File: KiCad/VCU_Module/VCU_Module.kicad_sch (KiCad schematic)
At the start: 5 parts, among them J1 5810132011, J5 pin header, J7 5V, J8 3V3, J9 GND

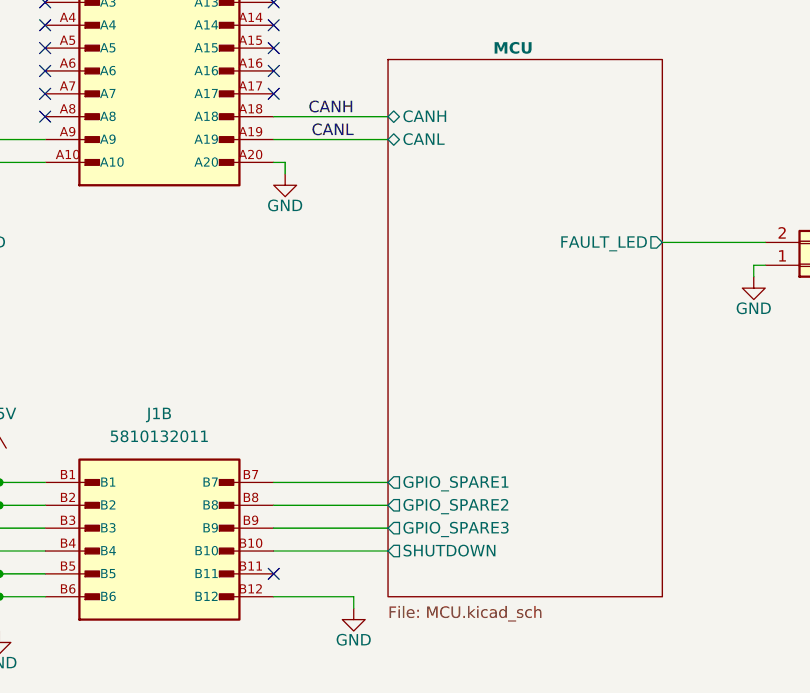
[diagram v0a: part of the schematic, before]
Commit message: added peripherals to mcu
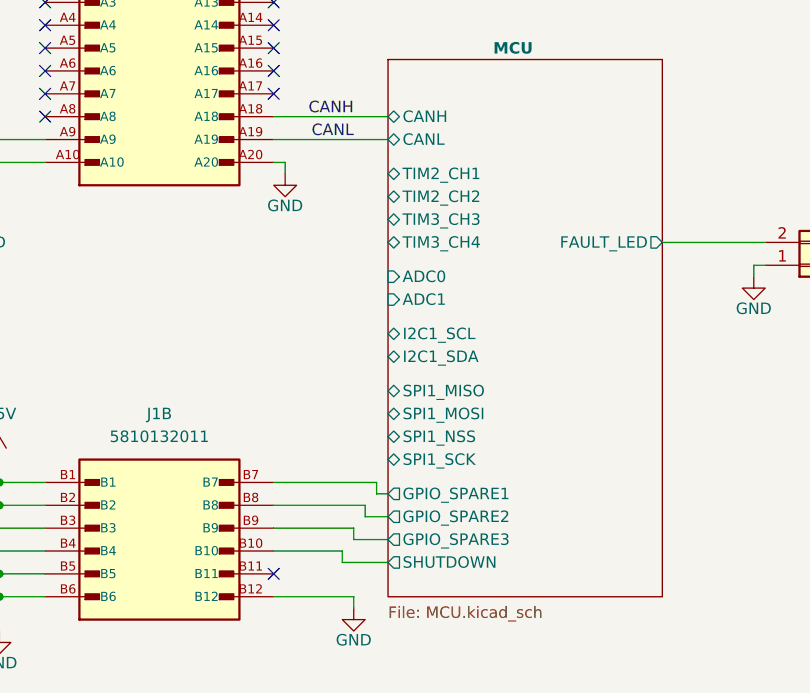
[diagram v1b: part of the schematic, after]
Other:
- sheet MCU ports: added ADC0, ADC1, I2C1_SCL, I2C1_SDA, SPI1_MISO, SPI1_MOSI, SPI1_NSS, SPI1_SCK, TIM2_CH1, TIM2_CH2, TIM3_CH3, TIM3_CH4; removed none
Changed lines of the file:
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@@
+	(wire
+		(pts
+			(xy 300.99 177.8) (xy 300.99 176.53)
+		)
+		(stroke
+			(width 0)
+			(type default)
+		)
+	)
+	(wire
+		(pts
+			(xy 297.18 185.42) (xy 297.18 184.15)
+		)
+		(stroke
+			(width 0)
+			(type default)
+		)
+	)
 	(wire
 		(pts
@@
 	(wire
 		(pts
+			(xy 299.72 180.34) (xy 299.72 179.07)
+		)
+		(stroke
+			(width 0)
+			(type default)
+		)
+	)
+	(wire
+		(pts
 			(xy 259.08 186.69) (xy 259.08 189.23)
 		)
@@
 	(wire
 		(pts
-			(xy 289.56 184.15) (xy 302.26 184.15)
+			(xy 297.18 185.42) (xy 302.26 185.42)
 		)
 		(stroke
@@
 	(wire
 		(pts
+			(xy 300.99 176.53) (xy 289.56 176.53)
+		)
+		(stroke
+			(width 0)
+			(type default)
+		)
+	)
+	(wire
+		(pts
 			(xy 346.71 106.68) (xy 345.44 106.68)
 		)
@@
 	(wire
 		(pts
-			(xy 289.56 176.53) (xy 302.26 176.53)
+			(xy 300.99 177.8) (xy 302.26 177.8)
 		)
 		(stroke
@@
 	(wire
 		(pts
-			(xy 289.56 179.07) (xy 302.26 179.07)
+			(xy 299.72 180.34) (xy 302.26 180.34)
 		)
 		(stroke
@@
 	(wire
 		(pts
+			(xy 298.45 182.88) (xy 298.45 181.61)
+		)
+		(stroke
+			(width 0)
+			(type default)
+		)
+	)
+	(wire
+		(pts
 			(xy 257.81 138.43) (xy 264.16 138.43)
 		)
@@
 	(wire
 		(pts
+			(xy 299.72 179.07) (xy 289.56 179.07)
+		)
+		(stroke
+			(width 0)
+			(type default)
+		)
+	)
+	(wire
+		(pts
 			(xy 259.08 173.99) (xy 259.08 176.53)
 		)
@@
 	(wire
 		(pts
-			(xy 289.56 181.61) (xy 302.26 181.61)
+			(xy 298.45 182.88) (xy 302.26 182.88)
 		)
 		(stroke
@@
 	(wire
 		(pts
+			(xy 298.45 181.61) (xy 289.56 181.61)
+		)
+		(stroke
+			(width 0)
+			(type default)
+		)
+	)
+	(wire
+		(pts
 			(xy 257.81 140.97) (xy 257.81 138.43)
 		)
@@
 		(pts
 			(xy 345.44 114.3) (xy 346.71 114.3)
+		)
+		(stroke
+			(width 0)
+			(type default)
+		)
+	)
+	(wire
+		(pts
+			(xy 297.18 184.15) (xy 289.56 184.15)
 		)
 		(stroke
@@
 		)
 		(pin "SHUTDOWN" output
-			(at 302.26 184.15 180)
+			(at 302.26 185.42 180)
 			(effects
 				(font
@@
 		)
 		(pin "GPIO_SPARE1" output
-			(at 302.26 176.53 180)
+			(at 302.26 177.8 180)
 			(effects
 				(font
@@
 		)
 		(pin "GPIO_SPARE3" output
-			(at 302.26 181.61 180)
+			(at 302.26 182.88 180)
 			(effects
 				(font
@@
 		)
 		(pin "GPIO_SPARE2" output
-			(at 302.26 179.07 180)
+			(at 302.26 180.34 180)
 			(effects
 				(font
@@
 			(effects
 				(font
+					(size 1.27 1.27)
+				)
+				(justify left)
+			)
+		)
+		(pin "ADC0" input
+			(at 302.26 153.67 180)
+			(effects
+				(font
+					(size 1.27 1.27)
+				)
+				(justify left)
+			)
+		)
+		(pin "ADC1" input
+			(at 302.26 156.21 180)
+			(effects
+				(font
+					(size 1.27 1.27)
+				)
+				(justify left)
+			)
+		)
+		(pin "I2C1_SCL" bidirectional
+			(at 302.26 160.02 180)
+			(effects
+				(font
+					(size 1.27 1.27)
+				)
+				(justify left)
+			)
+		)
+		(pin "I2C1_SDA" bidirectional
+			(at 302.26 162.56 180)
+			(effects
+				(font
+					(size 1.27 1.27)
+				)
+				(justify left)
+			)
+		)
+		(pin "SPI1_MISO" bidirectional
+			(at 302.26 166.37 180)
+			(effects
+				(font
+					(size 1.27 1.27)
+				)
+				(justify left)
+			)
+		)
+		(pin "SPI1_MOSI" bidirectional
+			(at 302.26 168.91 180)
+			(effects
+				(font
+					(size 1.27 1.27)
+				)
+				(justify left)
+			)
+		)
+		(pin "SPI1_NSS" bidirectional
+			(at 302.26 171.45 180)
+			(effects
+				(font
+					(size 1.27 1.27)
+				)
+				(justify left)
+			)
+		)
+		(pin "SPI1_SCK" bidirectional
+			(at 302.26 173.99 180)
+			(effects
+				(font
+					(size 1.27 1.27)
+				)
+				(justify left)
+			)
+		)
+		(pin "TIM2_CH1" bidirectional
+			(at 302.26 142.24 180)
+			(effects
+				(font
+					(size 1.27 1.27)
+				)
+				(justify left)
+			)
+		)
+		(pin "TIM2_CH2" bidirectional
+			(at 302.26 144.78 180)
+			(effects
+				(font
+					(size 1.27 1.27)
+				)
+				(justify left)
+			)
+		)
+		(pin "TIM3_CH3" bidirectional
+			(at 302.26 147.32 180)
+			(effects
+				(font
+					(size 1.27 1.27)
+				)
+				(justify left)
+			)
+		)
+		(pin "TIM3_CH4" bidirectional
+			(at 302.26 149.86 180)
+			(effects
+				(font

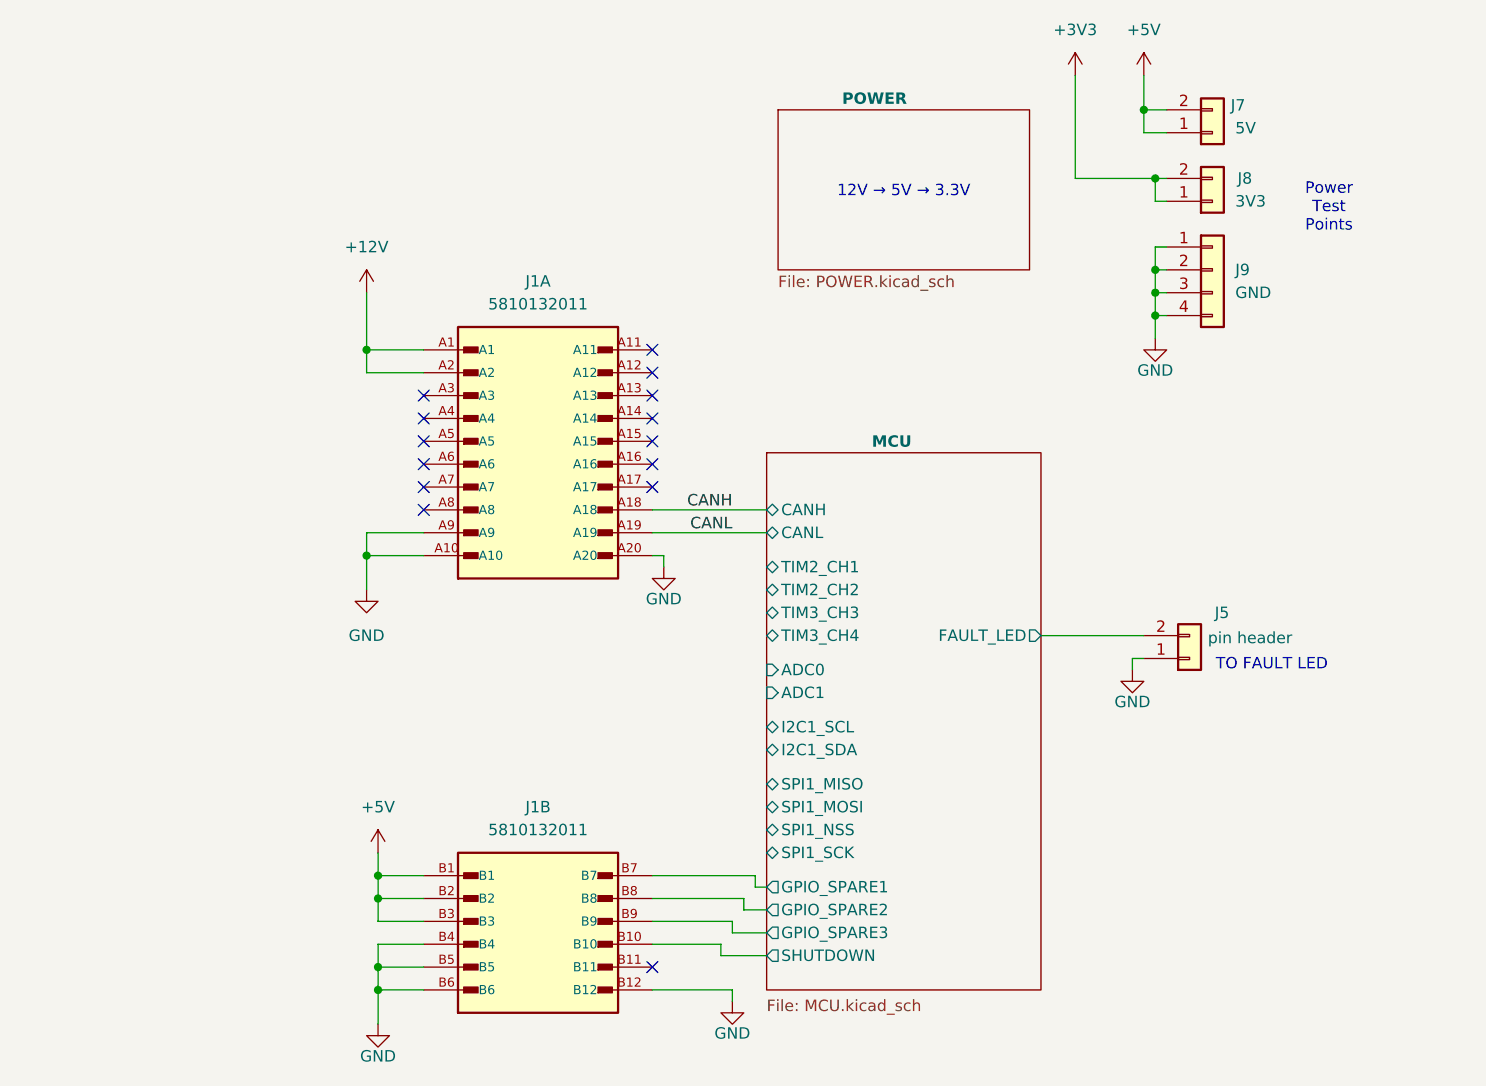
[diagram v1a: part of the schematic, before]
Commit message: added peripheral pins with the most functionality based on stm32c092rc datasheet, started placing components and routing traces on pcb
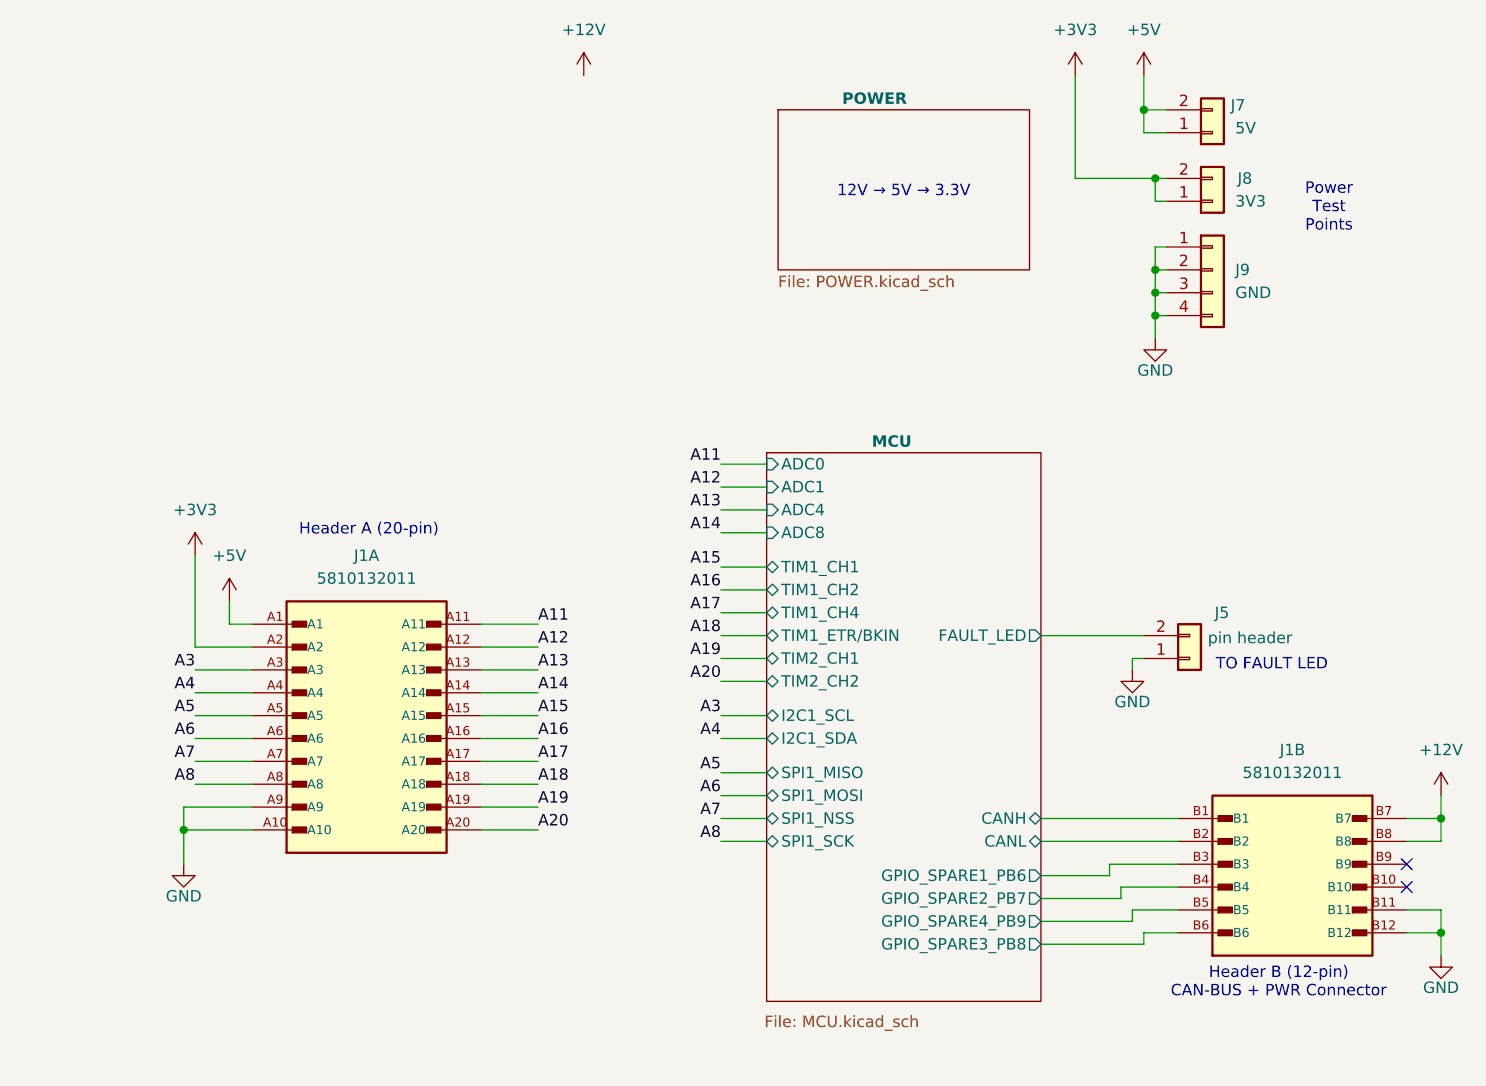
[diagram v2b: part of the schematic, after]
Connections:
- net MCU/GPIO_SPARE1 is gone; now on net +12V: J1.B7
- net MCU/GPIO_SPARE2 is gone; now on net +12V: J1.B8
- net +12V: no longer J1.A1, J1.A2
- net +3V3: now also J1.A2
- net +5V: now also J1.A1; no longer J1.B1, J1.B2, J1.B3
- net GND: now also J1.B11; no longer J1.A20, J1.B4, J1.B5, J1.B6
- net A11: now reaches J1.A11
- net A12: now reaches J1.A12
- net A13: now reaches J1.A13
- net A14: now reaches J1.A14
- net A15: now reaches J1.A15
- net A16: now reaches J1.A16
- net A17: now reaches J1.A17
- net A3: now reaches J1.A3
- net A4: now reaches J1.A4
- net A5: now reaches J1.A5
- net A6: now reaches J1.A6
- net A7: now reaches J1.A7
- net A8: now reaches J1.A8
- net CANH renamed A18
- net CANL renamed A19
- net MCU/GPIO_SPARE3: no longer names the net of J1.B9
- net MCU/SHUTDOWN: no longer names the net of J1.B10
- new net A20: J1.A20
- new net MCU/CANH: J1.B1
- new net MCU/CANL: J1.B2
- new net MCU/GPIO_SPARE1_PB6: J1.B3
- new net MCU/GPIO_SPARE2_PB7: J1.B4
- new net MCU/GPIO_SPARE3_PB8: J1.B6
- new net MCU/GPIO_SPARE4_PB9: J1.B5
- no-connect marks 14 -> 2
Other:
- sheet MCU ports: added ADC4, ADC8, GPIO_SPARE1_PB6, GPIO_SPARE2_PB7, GPIO_SPARE3_PB8, GPIO_SPARE4_PB9, TIM1_CH1, TIM1_CH2, TIM1_CH4, TIM1_ETR/BKIN; removed GPIO_SPARE1, GPIO_SPARE2, GPIO_SPARE3, SHUTDOWN, TIM3_CH3, TIM3_CH4
- note added: "Header A (20-pin)"
- note added: "Header B (12-pin) CAN-BUS + PWR Connector"
- moved on the sheet: J1A, J1B

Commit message: comments from andrew
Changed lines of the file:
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@@
-	)
-	(symbol
-		(lib_id "power:+12V")
-		(at 281.94 87.63 0)
-		(unit 1)
-		(body_style 1)
-		(exclude_from_sim no)
-		(in_bom yes)
-		(on_board yes)
-		(in_pos_files yes)
-		(dnp no)
-		(fields_autoplaced yes)
-		(property "Reference" "#PWR01"
-			(at 281.94 91.44 0)
-			(hide yes)
-			(show_name no)
-			(do_not_autoplace no)
-			(effects
-				(font
-					(size 1.27 1.27)
-				)
-			)
-		)
-		(property "Value" "+12V"
-			(at 281.94 82.55 0)
-			(show_name no)
-			(do_not_autoplace no)
-			(effects
-				(font
-					(size 1.27 1.27)
-				)
-			)
-		)
-		(property "Footprint" ""
-			(at 281.94 87.63 0)
-			(hide yes)
-			(show_name no)
-			(do_not_autoplace no)
-			(effects
-				(font
-					(size 1.27 1.27)
-				)
-			)
-		)
-		(property "Datasheet" ""
-			(at 281.94 87.63 0)
-			(hide yes)
-			(show_name no)
-			(do_not_autoplace no)
-			(effects
-				(font
-					(size 1.27 1.27)
-				)
-			)
-		)
-		(property "Description" "Power symbol creates a global label with name \"+12V\""
-			(at 281.94 87.63 0)
-			(hide yes)
-			(show_name no)
-			(do_not_autoplace no)
-			(effects
-				(font
-					(size 1.27 1.27)
-				)
-			)
-		)
-		(pin "1"
-		)
-		(instances
-			(project "VCU_Module"
-				(path "/efb70416-ce55-4766-98ba-c3d23efcccb1"
-					(reference "#PWR01")
-					(unit 1)
-				)
-			)
-		)
 	)
 	(symbol
